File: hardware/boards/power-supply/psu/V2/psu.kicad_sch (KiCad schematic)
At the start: 13 parts, among them U3 LM1117T-3.3

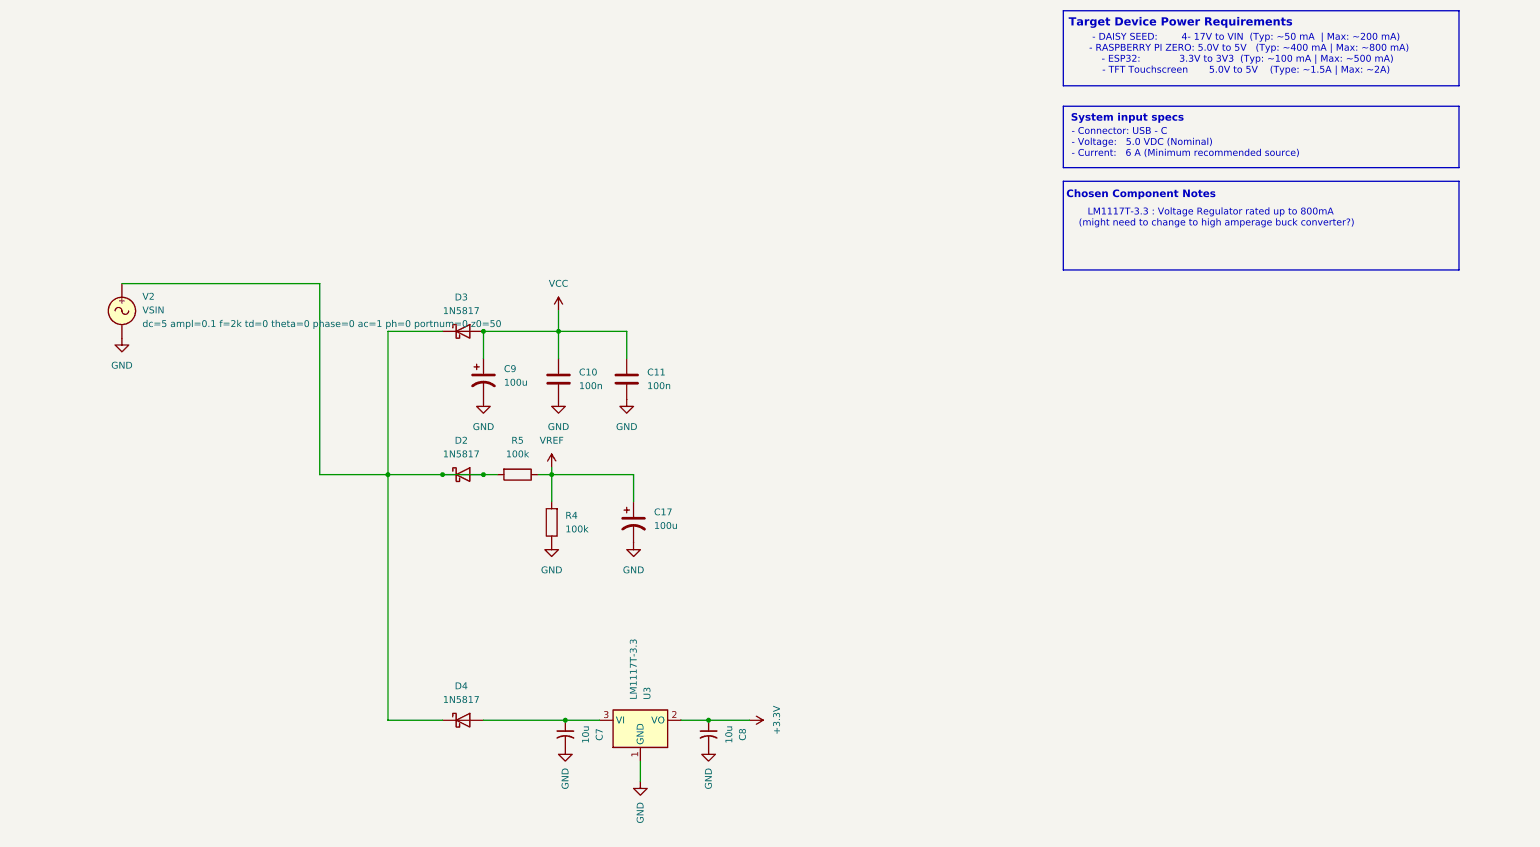
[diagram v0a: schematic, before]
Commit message: feat: update audio-daisy board schematic and add custom footprint library
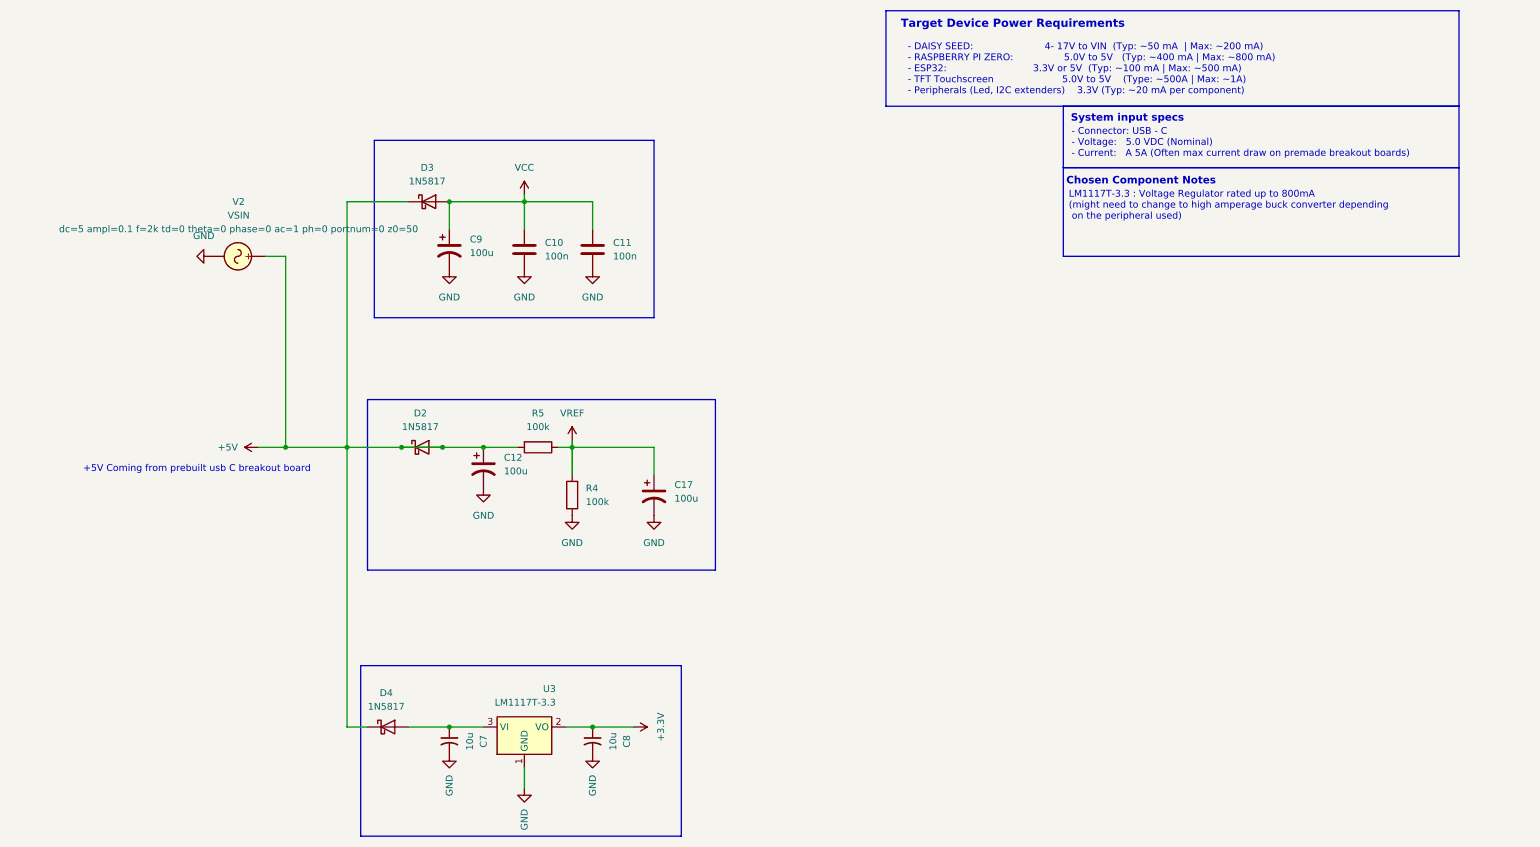
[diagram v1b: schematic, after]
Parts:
- added C12: 100u, symbol Device:C_Polarized_US
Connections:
- net GND: now also C12.2
- net +5V: now reaches D2.1 (K), D2.2 (A), D3.1 (K), D4.1 (K), R5.2, V2.1
- net +5V: now also C12.1
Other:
- note added: "+5V Coming from prebuilt usb C breakout board"
- note added: "- Connector: USB - C - Voltage: 5.0 VDC (Nominal) - Current: A 5A (Often max current draw on premade breakout boards)"
- note added: "- DAISY SEED: 4- 17V to VIN (Typ: ~50 mA | Max: ~200 mA) - RASPBERRY PI ZERO: 5.0V to 5V (Typ: ~400 mA | Max: ~800 mA) - ESP32: 3.3V or 5V (Typ: ~100 mA | Max: ~500 mA) - TFT Touchscreen 5.0V to 5V (Type: ~500A | Max: ~1A) - Peripherals (Led, I2C extenders) 3.3V (Typ: ~20 mA per component)"
- note added: "LM1117T-3.3 : Voltage Regulator rated up to 800mA (might need to change to high amperage buck converter depending on the peripheral used)"
- note removed: "- Connector: USB - C - Voltage: 5.0 VDC (Nominal) - Current: 6 A (Minimum recommended source)"
- note removed: "- DAISY SEED: 4- 17V to VIN (Typ: ~50 mA | Max: ~200 mA) - RASPBERRY PI ZERO: 5.0V to 5V (Typ: ~400 mA | Max: ~800 mA) - ESP32: 3.3V to 3V3 (Typ: ~100 mA | Max: ~500 mA) - TFT Touchscreen 5.0V to 5V (Type: ~1.5A | Max: ~2A)"
- note removed: "LM1117T-3.3 : Voltage Regulator rated up to 800mA (might need to change to high amperage buck converter?)"
- moved on the sheet: C10, C11, C17, C7, C8, C9, D2, D3, D4, R4, R5, U3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
